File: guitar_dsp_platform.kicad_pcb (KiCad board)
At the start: 2 copper layers, 122 x 122 mm, 108 parts, among them J201 694106301002, J401 NMJ6HCD2, J402 NMJ6HCD2, J403 NMJ6HCD2, J404 NMJ6HCD2, J501 I2S testpoint, U201 TLV1117-50, U202 TLV74133PDBVR, U203 LMR50410, U301 PCM3060, U401 OPA2197xD, U402 OPA2197xD, U403 OPA2197xD, U501 ESP32-DEVKIT-CVE

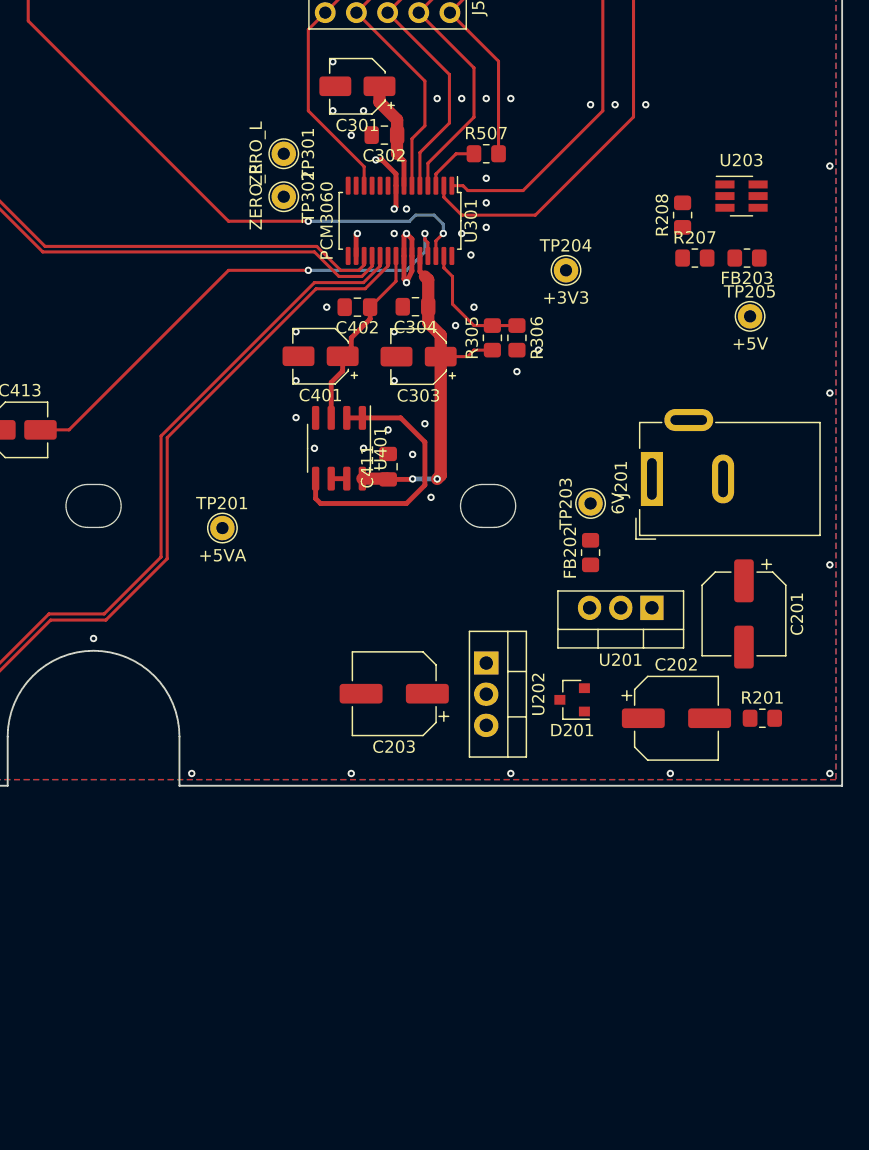
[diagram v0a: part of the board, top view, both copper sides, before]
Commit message: Add MIDI, convert to nightly kicad
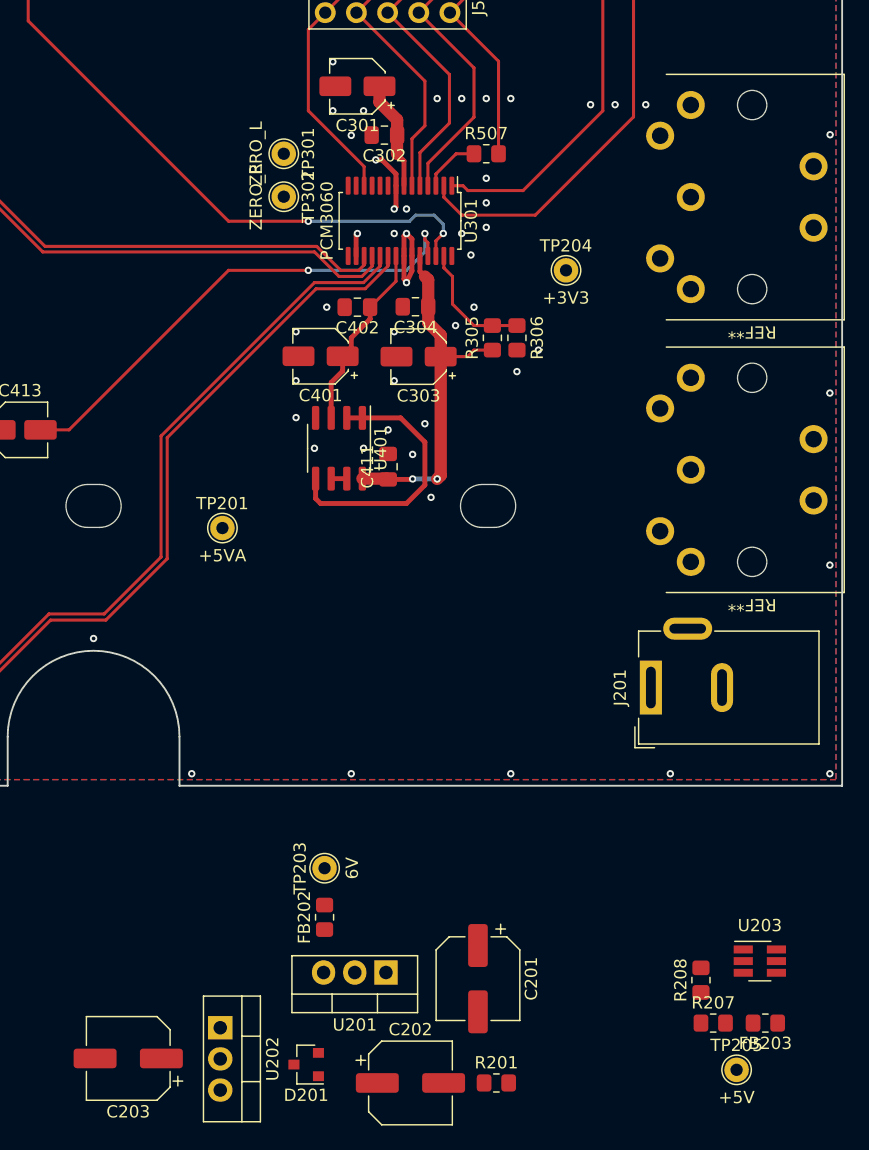
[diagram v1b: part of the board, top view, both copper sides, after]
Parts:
- added REF**: 57PC5F, guitar_dsp_platform:57PC5F, F.Cu at (153.7, 113.0)
- added REF**: 57PC5F, guitar_dsp_platform:57PC5F, F.Cu at (153.7, 135.3)
- moved FB203 62.4 mm to (154.7, 180.3)
- moved R207 62.4 mm to (150.5, 180.3)
- moved R208 62.4 mm to (149.5, 176.8)
- moved U203 62.4 mm to (154.3, 175.3)
- moved TP205 61.4 mm to (152.4, 184.2)
- moved C201 36.8 mm to (131.3, 176.7)
- moved R201 36.8 mm to (132.8, 185.2)
- moved C202 36.8 mm to (125.8, 185.2)
- moved C203 36.8 mm to (102.8, 183.2)
- moved D201 36.8 mm to (117.3, 183.7)
- moved FB202 36.8 mm to (118.8, 171.7)
- moved TP203 36.8 mm to (118.8, 167.7)
- moved U201 36.8 mm to (123.8, 176.2)
- moved U202 36.8 mm to (110.3, 180.7)
- moved J201 17.0 mm to (145.4, 153.0)
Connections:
- net /ESP32/~CODEC_RST renamed /ESP32/~{CODEC_RST}
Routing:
- net GND: vias 96 -> 102
- net GNDA: vias 6 -> 0
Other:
- copper layers 2 -> 4
- net class Default removed

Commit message: Review PSU, add footprints for all components
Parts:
- removed C406, C423, C424: 100n, Capacitor_SMD:C_0805_2012Metric_Pad1.18x1.45mm_HandSolder
- removed the FB201 at (89.5, 143.5)
- removed the R401 at (52.5, 45.0)
- removed R427, R428, R429, R430: 10k, Resistor_SMD:R_0805_2012Metric_Pad1.20x1.40mm_HandSolder
- removed REF** (x2): 57PC5F, guitar_dsp_platform:57PC5F
- added C214: 100n, Capacitor_SMD:C_0805_2012Metric_Pad1.18x1.45mm_HandSolder, F.Cu at (137.2, 50.8)
- added C401: 100n, Capacitor_SMD:C_0805_2012Metric_Pad1.18x1.45mm_HandSolder, F.Cu at (144.0, 135.1)
- added C402: 100n, Capacitor_SMD:C_0805_2012Metric_Pad1.18x1.45mm_HandSolder, F.Cu at (185.9, 103.9)
- added C502: 10u, Capacitor_SMD:C_1206_3216Metric_Pad1.33x1.80mm_HandSolder, F.Cu at (209.3, 162.8)
- added C503: 100n, Capacitor_SMD:C_0805_2012Metric_Pad1.18x1.45mm_HandSolder, F.Cu at (184.2, 135.1)
- added C504: 10u, Capacitor_SMD:C_1206_3216Metric_Pad1.33x1.80mm_HandSolder, F.Cu at (271.3, 122.9)
- added C506: 100n, Capacitor_SMD:C_0805_2012Metric_Pad1.18x1.45mm_HandSolder, F.Cu at (203.2, 161.0)
- added C507: 10u, Capacitor_SMD:C_1206_3216Metric_Pad1.33x1.80mm_HandSolder, F.Cu at (233.7, 147.6)
- added C508: 10u, Capacitor_SMD:C_1206_3216Metric_Pad1.33x1.80mm_HandSolder, F.Cu at (211.8, 162.8)
- added C509: 10u, Capacitor_SMD:C_1206_3216Metric_Pad1.33x1.80mm_HandSolder, F.Cu at (214.3, 162.8)
- added C510: 10u, Capacitor_SMD:C_1206_3216Metric_Pad1.33x1.80mm_HandSolder, F.Cu at (232.2, 154.7)
- added C512: 100u, Capacitor_SMD:CP_Elec_6.3x7.7, F.Cu at (226.3, 138.2)
- added D401: BAT54S, Package_TO_SOT_SMD:SOT-23, F.Cu at (233.9, 100.1)
- added D502: ZMM5242B, Diode_SMD:D_MiniMELF, F.Cu at (190.8, 136.1)
- added FB401: 600R@100MHz, Resistor_SMD:R_0805_2012Metric_Pad1.20x1.40mm_HandSolder, F.Cu at (229.9, 98.3)
- added FB402: 600R@100MHz, Resistor_SMD:R_0805_2012Metric_Pad1.20x1.40mm_HandSolder, F.Cu at (226.1, 100.3)
- added FB403: 600R@100MHz, Resistor_SMD:R_0805_2012Metric_Pad1.20x1.40mm_HandSolder, F.Cu at (217.4, 104.1)
- added FB404: 600R@100MHz, Resistor_SMD:R_0805_2012Metric_Pad1.20x1.40mm_HandSolder, F.Cu at (221.5, 116.3)
- added FB502: 600R@100MHz, Resistor_SMD:R_0805_2012Metric_Pad1.20x1.40mm_HandSolder, F.Cu at (187.5, 135.1)
- added J401: 57PC5F, guitar_dsp_platform:57PC5F, F.Cu at (153.4, 135.1)
- added J402: 57PC5F, guitar_dsp_platform:57PC5F, F.Cu at (153.4, 114.6)
- added L501: 15uH, Inductor_SMD:L_Bourns-SRN8040_8x8.15mm, F.Cu at (210.1, 153.4)
- added Q401: 2N3904, Package_TO_SOT_THT:TO-92_Inline, F.Cu at (217.2, 97.1)
- added Q501: DMG2307LQ, Package_TO_SOT_SMD:SOT-23, F.Cu at (193.8, 136.1)
- added R212: 820, Resistor_SMD:R_0805_2012Metric_Pad1.20x1.40mm_HandSolder, F.Cu at (46.0, 46.7)
- added R219: 22k, Resistor_SMD:R_0805_2012Metric_Pad1.20x1.40mm_HandSolder, F.Cu at (46.0, 42.9)
- added R220: 22k, Resistor_SMD:R_0805_2012Metric_Pad1.20x1.40mm_HandSolder, F.Cu at (43.9, 42.9)
- added R227: 10k, Resistor_SMD:R_0805_2012Metric_Pad1.20x1.40mm_HandSolder, F.Cu at (49.0, 41.9)
- added R228: 820, Resistor_SMD:R_0805_2012Metric_Pad1.20x1.40mm_HandSolder, F.Cu at (52.1, 46.7)
- added R229: 22k, Resistor_SMD:R_0805_2012Metric_Pad1.20x1.40mm_HandSolder, F.Cu at (52.1, 42.9)
- added R230: 820, Resistor_SMD:R_0805_2012Metric_Pad1.20x1.40mm_HandSolder, F.Cu at (58.2, 46.7)
- added R231: 22k, Resistor_SMD:R_0805_2012Metric_Pad1.20x1.40mm_HandSolder, F.Cu at (58.2, 42.9)
- added R232: 10k, Resistor_SMD:R_0805_2012Metric_Pad1.20x1.40mm_HandSolder, F.Cu at (61.2, 41.9)
- added R233: 820, Resistor_SMD:R_0805_2012Metric_Pad1.20x1.40mm_HandSolder, F.Cu at (64.3, 46.7)
- added R234: 22k, Resistor_SMD:R_0805_2012Metric_Pad1.20x1.40mm_HandSolder, F.Cu at (64.3, 42.9)
- added R303: 10k, Resistor_SMD:R_0805_2012Metric_Pad1.20x1.40mm_HandSolder, F.Cu at (110.0, 96.5)
- added R405: 7.5k, Resistor_SMD:R_0805_2012Metric_Pad1.20x1.40mm_HandSolder, F.Cu at (217.4, 102.1)
- added R406: 10, Resistor_SMD:R_0805_2012Metric_Pad1.20x1.40mm_HandSolder, F.Cu at (220.5, 103.1)
- added R412: 33 0.5W, Resistor_SMD:R_1206_3216Metric_Pad1.30x1.75mm_HandSolder, F.Cu at (216.9, 114.3)
- added R501: 1Meg, Resistor_SMD:R_0805_2012Metric_Pad1.20x1.40mm_HandSolder, F.Cu at (198.9, 162.6)
- added R502: 200k, Resistor_SMD:R_0805_2012Metric_Pad1.20x1.40mm_HandSolder, F.Cu at (198.9, 164.6)
- added R504: 121k, Resistor_SMD:R_0805_2012Metric_Pad1.20x1.40mm_HandSolder, F.Cu at (216.4, 162.8)
- added R505: 22.1k, Resistor_SMD:R_0805_2012Metric_Pad1.20x1.40mm_HandSolder, F.Cu at (218.4, 162.8)
- added R508: 10k, Resistor_SMD:R_0805_2012Metric_Pad1.20x1.40mm_HandSolder, F.Cu at (187.5, 137.2)
- added R509: 33, Resistor_SMD:R_0805_2012Metric_Pad1.20x1.40mm_HandSolder, F.Cu at (234.2, 143.0)
- added U402: 6N138, Package_DIP:DIP-8_W8.89mm_SMDSocket_LongPads, F.Cu at (243.1, 99.8)
- R205: renamed from R410; value R -> DNF
- R206: renamed from R409; value R -> DNF
- R207: renamed from R412; value R -> DNF
- R208: renamed from R411; value R -> DNF
- R403: value 10k -> 220
- R404: value 10k -> 820
- TP502: renamed from TP203; value 6V -> +6V
- U401: renamed from U501; value ESP32-DEVKIT-CVE -> ESP32-DEVKITC-VE
- U502: renamed from U201; footprint Package_TO_SOT_THT:TO-220-3_Vertical -> Package_TO_SOT_SMD:SOT-223-3_TabPin2
- U503: renamed from U202; footprint Package_TO_SOT_THT:TO-220-3_Vertical -> Package_TO_SOT_SMD:SOT-23-5
- moved R404 187.9 mm to (238.7, 110.2), turned to 0 degrees
- moved R403 187.7 mm to (229.9, 100.3), turned to 0 degrees
- moved C403 186.4 mm to (221.5, 114.3), turned to 0 degrees
- moved D501 161.7 mm to (265.9, 119.9), turned to 0 degrees
- moved TP502 161.6 mm to (272.5, 117.9)
- moved FB501 160.8 mm to (271.3, 120.7), turned to 0 degrees
- moved U502 148.8 mm to (263.8, 125.7)
- moved C505 141.4 mm to (255.3, 128.3), turned to -90 degrees
- moved C511 140.2 mm to (239.5, 151.9), turned to 0 degrees
- moved R503 132.2 mm to (255.3, 135.3), turned to -90 degrees
- moved U503 125.4 mm to (232.2, 151.1)
- moved TP504 120.8 mm to (255.3, 120.9)
- moved FB503 86.9 mm to (234.2, 145.1)
- moved R507 85.7 mm to (229.9, 147.1)
- moved R506 84.2 mm to (227.8, 147.1), turned to 90 degrees
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- renumbered C401 to C201, C402 to C202, C404 to C203, C405 to C204, C407 to C205, C410 to C206, C409 to C207, C408 to C208, C411 to C209, C412 to C210, C413 to C211, C415 to C212, C416 to C213, C417 to C216, C418 to C217, C419 to C218, C420 to C219, C422 to C220, C421 to C221, C201 to C501, C202 to C505, C203 to C511, D401 to D201, D402 to D202, D404 to D203, D403 to D204, D201 to D501, FB402 to FB201, FB401 to FB202, FB202 to FB501, FB203 to FB503, J402 to J201, J401 to J202, J404 to J203, J403 to J204, J501 to J403, J201 to J501, R405 to R201, R406 to R202, R408 to R203, R407 to R204, R413 to R209, R414 to R210, R402 to R211, R415 to R213, R416 to R214, R417 to R215, R418 to R216, R419 to R217, R420 to R218, R421 to R221, R422 to R222, R423 to R223, R424 to R224, R425 to R225, R426 to R226, R305 to R301, R306 to R302, R504 to R401, R505 to R402, R501 to R407, R502 to R408, R503 to R409, R506 to R410, R507 to R411, R201 to R503, R207 to R506, R208 to R507, TP401 to TP201, TP402 to TP202, TP403 to TP203, TP404 to TP204, TP405 to TP205, TP406 to TP206, TP201 to TP501, TP204 to TP503, TP205 to TP504, U402 to U201, U403 to U202, U401 to U203, U203 to U501
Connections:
- net /Analogue/VCOM_CODEC renamed /Audio Codec/VCOM_CODEC
- net /Analogue/VINL renamed /Audio Codec/VINL
- net /Analogue/VINR renamed /Audio Codec/VINR
- net /Audio Codec/BCK renamed /ESP32/BCK
- net /Audio Codec/DAC_DATA renamed /ESP32/DAC_DATA
- net /Audio Codec/LRCK renamed /ESP32/LRCK
- net /Audio Codec/SCK renamed /ESP32/SCK
- net /ESP32/~{CODEC_RST} renamed /Audio Codec/~{RST}
- net VCOM renamed /Analogue/Vref
- C403 pad 1: /Analogue/PRE_IN_DET -> Net-(C403-Pad1)
- C501 pad 1: +VDC -> /Power Supplies/VDC_F
- D501 pad 2: +VDC -> /Power Supplies/+6V_F
- D501 pad 3: +5VA -> +5V
- FB501 pad 1: Net-(C209-Pad1) -> /Power Supplies/+6V_F
- FB503 pad 1: Net-(C211-Pad1) (its old number) -> /Power Supplies/+5V_F
- J201 pad R: Net-(J402-PadR) -> unconnected-(J201-PadR)
- J201 pad RN: Net-(J402-PadRN) -> unconnected-(J201-PadRN)
- J202 pad R: Net-(J401-PadR) -> unconnected-(J202-PadR)
- J202 pad RN: Net-(J401-PadRN) -> unconnected-(J202-PadRN)
- J203 pad R: Net-(J404-PadR) -> unconnected-(J203-PadR)
- J203 pad RN: Net-(J404-PadRN) -> unconnected-(J203-PadRN)
- J203 pad TN: Net-(J404-PadTN) -> unconnected-(J203-PadTN)
- J204 pad R: Net-(J403-PadR) -> unconnected-(J204-PadR)
- J204 pad RN: Net-(J403-PadRN) -> unconnected-(J204-PadRN)
- J204 pad TN: Net-(J403-PadTN) -> unconnected-(J204-PadTN)
- J501 pad 1: +VDC -> /Power Supplies/VDC_IN
- R211 pad 1: +3V3 -> Net-(R211-Pad1)
- R211 pad 2: /Analogue/G_DET_JACK -> Net-(R211-Pad2)
- R401 pad 1: +3V3 -> VDD
- R403 pad 1: /Analogue/PRE_IN_DET -> Net-(FB402-Pad1)
- R403 pad 2: /Analogue/PRE_I_DET_JACK -> /ESP32/LED-
- R404 pad 1: /Analogue/G_DET -> /ESP32/MIDI_RX_uC
- R404 pad 2: /Analogue/G_DET_JACK -> VDD
- U401 pad 1: Net-(U501-Pad1) -> VDD
- U401 pad 10: /ESP32/IO26 -> /ESP32/MIDI_RX_uC
- U401 pad 27: Net-(U501-Pad27) -> unconnected-(U401-Pad27)
- U401 pad 28: Net-(U501-Pad28) -> unconnected-(U401-Pad28)
- U401 pad 3: /Analogue/PRE_OUT_DET -> /ESP32/I2
- U401 pad 4: /Analogue/PRE_IN_DET -> /ESP32/I3
- U401 pad 5: /Analogue/AMP_DET -> /ESP32/I1
- U401 pad 6: /Analogue/G_DET -> /Analogue/JACK_DETECT
- U401 pad 9: /ESP32/IO25 -> /ESP32/MIDI_TX_uC
- U501 pad 5: +VDC -> /Power Supplies/VDC_F
- U502 pad 3: Net-(C209-Pad1) -> /Power Supplies/+6V_F
- U503 pad 1: Net-(C211-Pad1) (its old number) -> /Power Supplies/+5V_F
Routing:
- net /Analogue/PRE_OUT_DET: track 110.8 -> 0.00 mm
- net /Analogue/PRE_IN_DET: track 101.5 -> 0.00 mm
- net /Analogue/AMP_DET: track 92.5 -> 0.00 mm
- net /Analogue/JACK_DETECT: track 0.00 -> 84.2 mm
- net /Analogue/G_DET: track 80.9 -> 0.00 mm
- net VDD: track 0.00 -> 24.4 mm, vias 0 -> 4
- net /Analogue/PRE_O_DET_JACK: track 28.9 -> 46.8 mm
- net /Analogue/PRE_I_DET_JACK: track 55.4 -> 68.9 mm
- net /Analogue/AMP_DET_JACK: track 80.8 -> 90.6 mm
- net Net-(D502-Pad2): track 0.00 -> 8.49 mm
- net +VDC: track 0.00 -> 6.75 mm
- net /Power Supplies/VDC_F: track 0.00 -> 4.34 mm
- net /Analogue/G_DET_JACK: track 19.2 -> 23.4 mm
- net Net-(R211-Pad1): track 0.00 -> 4.11 mm
- net Net-(R211-Pad2): track 0.00 -> 4.11 mm
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- added copper zone on In1.Cu, net GND
- added copper zone on In2.Cu, net GND

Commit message: Tweak layout
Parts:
- removed TP301: ZERO_L, guitar_dsp_platform:TestPoint_THTPad_D2.0mm_Drill1.0mm
- removed TP302: ZERO_R, guitar_dsp_platform:TestPoint_THTPad_D2.0mm_Drill1.0mm
- moved TP502 165.5 mm to (110.8, 152.8), turned to 0 degrees
- moved C504 157.3 mm to (114.0, 122.8)
- moved D501 157.3 mm to (108.7, 119.7)
- moved FB501 157.3 mm to (114.0, 120.5)
- moved U502 157.3 mm to (106.5, 125.5)
- moved TP504 150.8 mm to (104.5, 119.8)
- moved R503 146.4 mm to (109.0, 131.3), turned to 0 degrees
- moved C505 139.8 mm to (115.5, 129.3)
- moved C507 109.6 mm to (126.7, 124.1)
- moved C510 109.6 mm to (125.2, 131.2)
- moved C511 109.6 mm to (132.5, 128.4)
- moved R506 109.6 mm to (120.8, 123.6)
- moved R507 109.6 mm to (122.9, 123.6)
- moved U503 109.6 mm to (125.2, 127.6)
- moved FB503 109.6 mm to (127.2, 121.6)
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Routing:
- net /Analogue/Vref: track 22.0 -> 374.0 mm, vias 0 -> 9
- net VDD: track 24.4 -> 155.1 mm, vias 4 -> 7
- net +5VA: track 65.2 -> 160.7 mm, vias 2 -> 5
- net /Audio Codec/~{RST}: track 0.00 -> 62.2 mm
- net /Audio Codec/SCL: track 48.0 -> 0.00 mm
- net /Audio Codec/SDA: track 42.3 -> 0.00 mm
- net /Audio Codec/VINR: track 64.6 -> 32.5 mm
- net /Analogue/VOUTR+: track 59.3 -> 30.5 mm
- net /Analogue/VOUTR-: track 57.0 -> 29.0 mm
- net /ESP32/ADC_DATA_uC: track 34.3 -> 55.3 mm
- net /ESP32/LRCK: track 25.3 -> 42.1 mm
- net Net-(FB201-Pad2): track 15.8 -> 30.4 mm
- net Net-(C210-Pad1): track 7.03 -> 19.2 mm
- net /ESP32/BCK: track 24.7 -> 36.7 mm
- net Net-(C218-Pad1): track 35.0 -> 42.7 mm
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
